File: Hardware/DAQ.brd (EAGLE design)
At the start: 44.4 x 39.7 mm, 35 parts, among them U1 DAC8564IAPW, U2 AD7606BSTZ

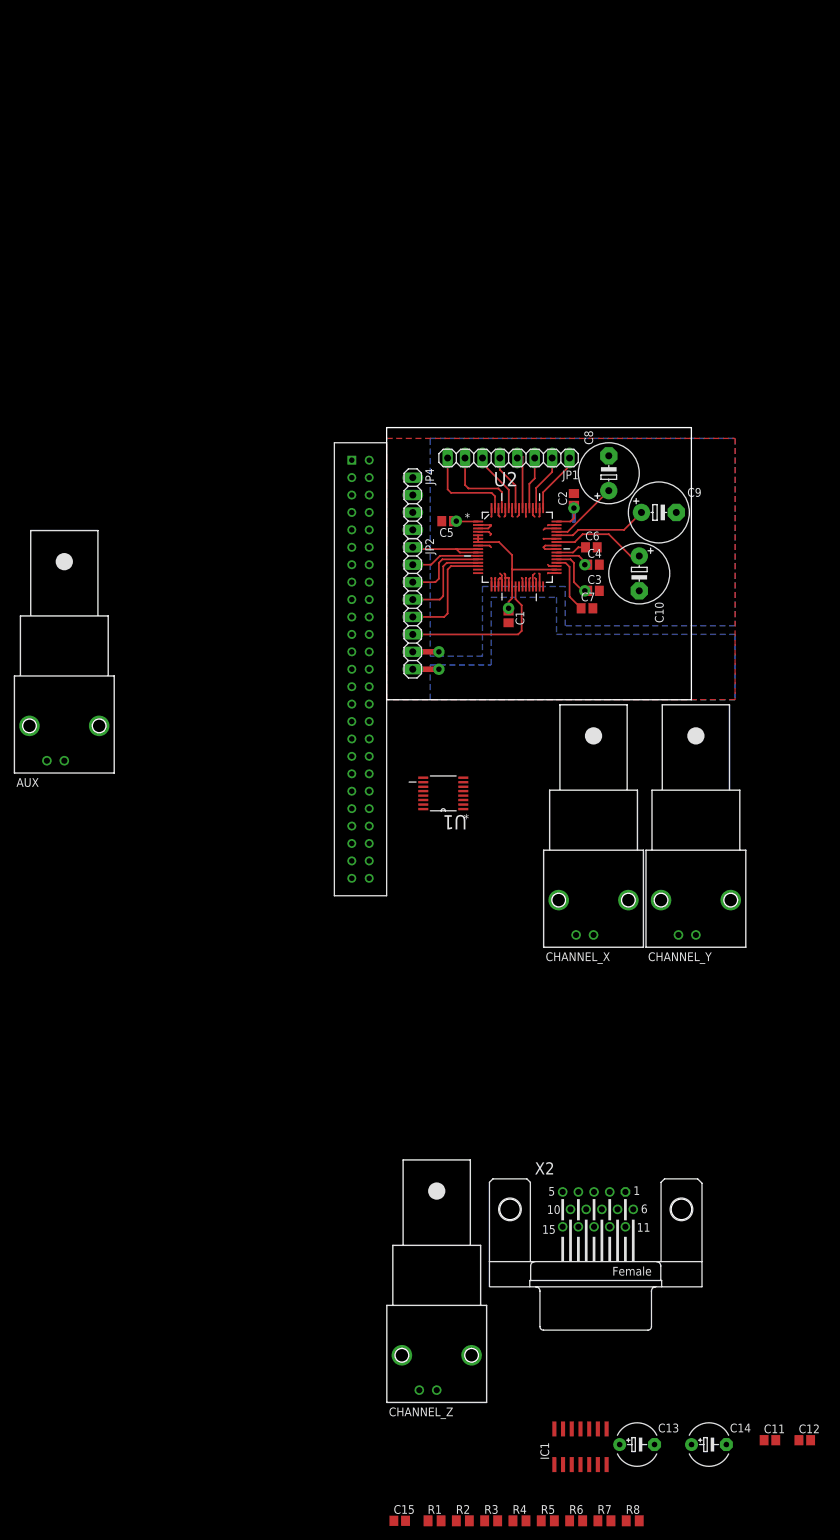
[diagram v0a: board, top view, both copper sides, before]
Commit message: added usart interface
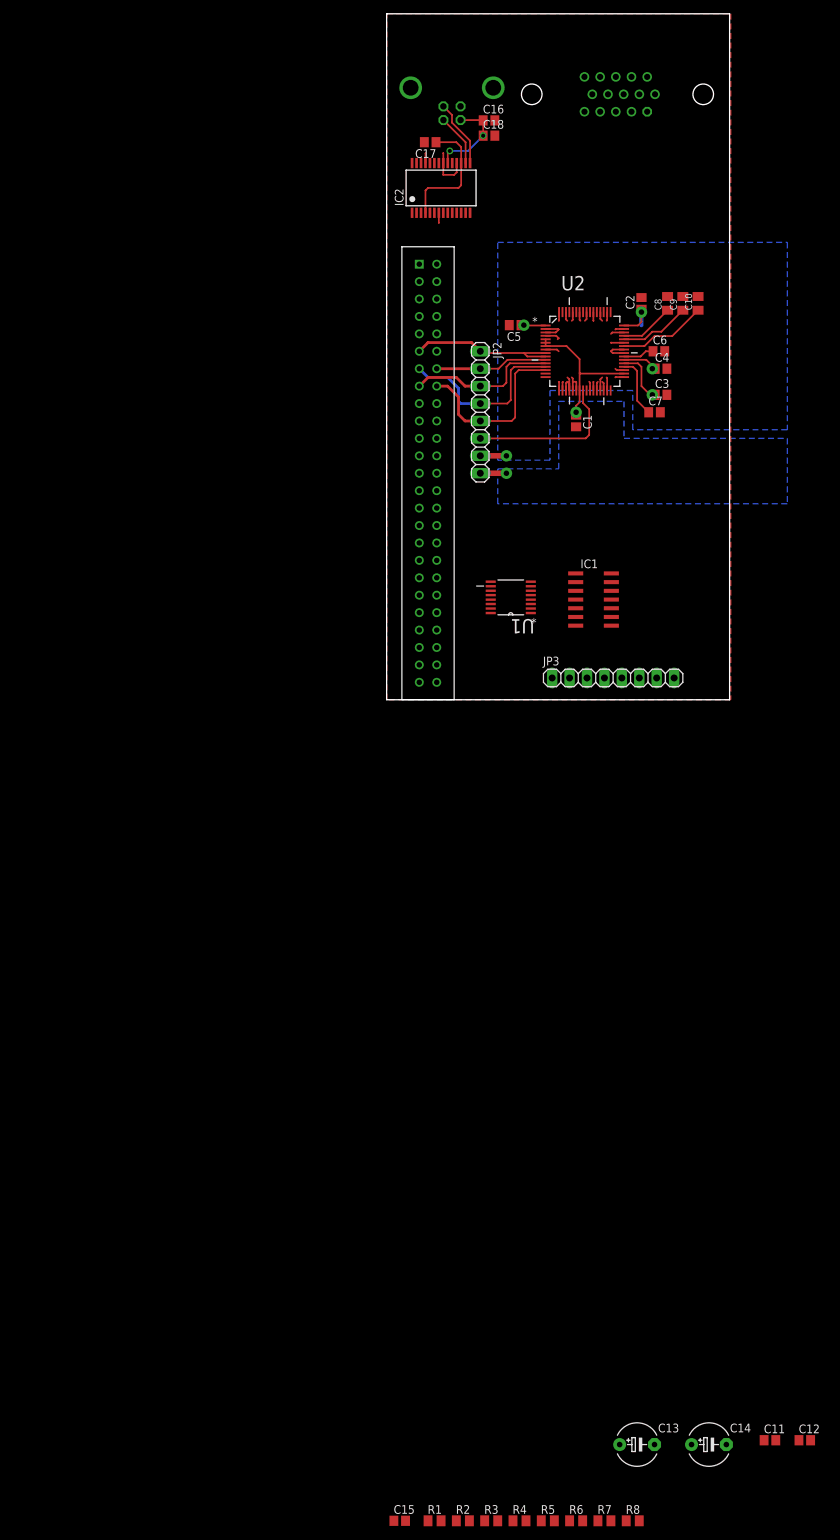
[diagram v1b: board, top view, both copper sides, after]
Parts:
- removed AUX, CHANNEL_X, CHANNEL_Y, CHANNEL_Z: (no value), con-coax:AMP_227161
- removed JP1: (no value), pinhead:1X08
- removed JP4: (no value), pinhead:1X04
- added C16, C17, C18: (no value), resistor:C0805
- added IC2: FT232RL, ftdichip:SSOP28
- added JP3: (no value), pinhead:1X08
- added X1: PN61729-S, con-berg:PN61729-S
- C10, C8, C9: device resistor:E5-8,5 -> resistor:C0805K
- moved X2 162.6 mm to (33.7, 88.3), flipped to the bottom, turned to 180 degrees
- moved IC1 123.5 mm to (30.2, 14.6), turned to 270 degrees
- moved C10 40.3 mm to (45.4, 57.8), turned to 90 degrees
- moved C9 30.7 mm to (43.2, 57.8), turned to 90 degrees
- moved C1 30.2 mm to (27.6, 40.6)
- moved C3 30.2 mm to (40.0, 44.5)
- moved U$1 30.2 mm to (6.03, 33.0)
- moved C4 30.2 mm to (40.0, 48.3)
- moved C5 30.2 mm to (18.7, 54.6)
- moved U1 30.2 mm to (18.1, 14.9)
- moved C2 30.2 mm to (37.1, 57.8)
- moved C6 30.2 mm to (39.7, 50.8)
- moved C7 30.2 mm to (39.1, 41.9)
- moved JP2 30.2 mm to (13.7, 41.9)
- moved U2 30.2 mm to (28.9, 50.8)
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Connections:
- removed net AGND: C1.2, C10.-, C2.2, C3.2, C4.2, C5.2, C6.2, C7.2, C8.-, C9.-, JP4.1, JP4.2, JP4.3, JP4.4, U2.16, U2.17, U2.18, U2.19, U2.2, U2.20, U2.21, U2.22, U2.26, U2.27, U2.28, U2.29, U2.3, U2.30, U2.31, U2.33, U2.35, U2.4, U2.40, U2.41, U2.43, U2.46, U2.47, U2.50, U2.52, U2.54, U2.56, U2.58, U2.60, U2.62, U2.64, U2.8
- removed net N$12: JP1.2, U2.51
- removed net N$13: JP1.5, U2.57
- removed net N$14: JP1.6, U2.59
- removed net N$4: JP1.3, U2.53
- removed net SP1_SCLK: JP2.3, U2.12
- net GND: now also C1.2, C10.2, C16.2, C17.2, C18.2, C2.2, C3.2, C4.2, C5.2, C6.2, C7.2, C8.2, C9.2, IC2.18, IC2.21, IC2.25, IC2.26, IC2.7, JP3.2, JP3.4, JP3.6, JP3.8, U2.16, U2.17, U2.18, U2.19, U2.2, U2.20, U2.21, U2.22, U2.26, U2.27, U2.28, U2.29, U2.3, U2.30, U2.31, U2.33, U2.35, U2.4, U2.40, U2.41, U2.43, U2.46, U2.47, U2.50, U2.52, U2.54, U2.56, U2.58, U2.60, U2.62, U2.64, U2.8, X1.4, X1.S1, X1.S2; no longer AUX.2, CHANNEL_X.2, CHANNEL_Y.2, CHANNEL_Z.2
- net N$1: now also C16.1, C18.1, IC2.20, X1.1; no longer JP1.8, U2.63
- net N$11: now also C17.1, IC2.17, IC2.4; no longer JP1.1, U2.49
- net N$15: now also C10.1; no longer C10.+
- net N$19: now also JP3.1; no longer CHANNEL_X.1
- net N$2: now also IC2.16, X1.2; no longer JP1.4, U2.55
- net N$21: now also JP3.3; no longer CHANNEL_Y.1
- net N$23: now also JP3.5; no longer CHANNEL_Z.1
- net N$25: now also JP3.7; no longer AUX.1
- net N$3: now also IC2.15, X1.3; no longer JP1.7, U2.61
- net N$8: now also C8.1; no longer C8.+
- net N$9: now also C9.1; no longer C9.+
- net Q1-Q2_BUF: now also U2.49
- net Q1-Q4_BUF: now also U2.53
- net Q1_BUF: now also U2.55
- net Q2-Q3_BUF: now also U2.63
- net Q2_BUF: now also U2.57
- net Q3_BUF: now also U2.59
- net Q4-Q3_BUF: now also U2.51
- net Q4_BUF: now also U2.61
- net SPI1_SCLK: now also JP2.3, U2.12
- net USART3_RX: now also IC2.1
- net USART3_TX: now also IC2.5
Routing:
- net GND: track 0.00 -> 60.7 mm
- net AGND: track 51.1 -> 0.00 mm
- net SPI1_SCLK: track 0.00 -> 22.8 mm
- net SP1_SCLK: track 12.3 -> 0.00 mm
- net CS: track 14.3 -> 26.4 mm
- net CONVST: track 12.9 -> 22.9 mm
- net BUSY: track 16.3 -> 26.3 mm
- net N$11: track 8.90 -> 18.3 mm
- net N$14: track 8.89 -> 0.00 mm
- net N$12: track 8.27 -> 0.00 mm
- net N$13: track 8.25 -> 0.00 mm
- net N$4: track 7.63 -> 0.00 mm
- net RESET: track 10.1 -> 16.4 mm
- net N$9: track 13.8 -> 10.3 mm
- net N$8: track 10.1 -> 7.89 mm
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- added copper zone on layer 1, net GND
- removed copper zone on layer 1, net AGND
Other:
- board size 44.4 x 39.7 mm -> 50 x 100 mm

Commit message: finished board layout
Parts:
- removed JP2: (no value), pinhead:1X08
- added C19, C20, C21, C22, C23, C24, C25, C26: (no value), resistor:C0805K
- added D1: 1N4004, diode:DO41-10
- added IC3, IC4, IC5: MCP1703DB, linear:SOT223
- added JP1: (no value), pinhead:1X02
- added JP4: (no value), pinhead:1X03
- C13, C14: device resistor:E5-6 -> resistor:C0805
- moved C15 149.7 mm to (17.1, 29.2), turned to 180 degrees
- moved R7 144.0 mm to (38.1, 24.1), turned to 270 degrees
- moved R8 143.9 mm to (40.3, 24.1), turned to 90 degrees
- moved R1 143.7 mm to (27.3, 22.5), turned to 90 degrees
- moved R2 142.9 mm to (25.1, 22.5), turned to 270 degrees
- moved C12 142.7 mm to (31.8, 31.8)
- moved C14 139.0 mm to (31.8, 29.5)
- moved C11 137.4 mm to (31.8, 27.3)
- moved C13 136.9 mm to (17.1, 27.0), turned to 180 degrees
- moved R3 135.2 mm to (27.3, 14.9), turned to 90 degrees
- moved R4 134.7 mm to (25.1, 14.9), turned to 270 degrees
- moved R5 134.1 mm to (38.1, 13.7), turned to 270 degrees
- moved R6 134.0 mm to (40.3, 13.7), turned to 90 degrees
- moved U1 16.0 mm to (23.8, 29.8)
- moved C7 14.9 mm to (39.1, 56.8)
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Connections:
- removed net V+: IC1.4
- removed net V-: IC1.11
- new net N$12: C21.1, IC5.3, JP1.1
- new net N$29: C22.1, C23.1, C24.1, D1.C, IC3.1, IC4.1, IC5.1
- net +15V: now also C25.1, D1.A, IC1.4, JP4.1
- net +3V3: now also C13.1, C14.1, C20.1, IC3.3; no longer C13.+, C14.+, JP2.8
- net +5V: now also C19.1, IC4.3; no longer JP2.7
- net -15V: now also C26.1, IC1.11, JP4.3
- net BUSY: no longer JP2.5
- net CONVST: no longer JP2.1
- net CS: no longer JP2.4
- net GND: now also C13.2, C14.2, C19.2, C20.2, C21.2, C22.2, C23.2, C24.2, C25.2, C26.2, IC3.2, IC4.2, IC5.2, JP1.2, JP4.2; no longer C13.-, C14.-
- net RESET: no longer JP2.2
- net SPI1_MISO: no longer JP2.6
- net SPI1_SCLK: no longer JP2.3
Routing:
- net +15V: track 0.00 -> 145.9 mm, vias 0 -> 2
- net -15V: track 0.00 -> 118.2 mm, vias 0 -> 1
- net N$29: track 0.00 -> 72.5 mm, vias 0 -> 2
- net USART3_TX: track 0.00 -> 63.3 mm
- net USART3_RX: track 0.00 -> 60.7 mm
- net N$25: track 0.00 -> 47.7 mm
- net N$19: track 0.00 -> 34.4 mm
- net SPI2_MOSI: track 0.00 -> 31.0 mm
- net Q4_BUF: track 0.00 -> 29.5 mm
- net N$16: track 0.00 -> 29.4 mm, vias 0 -> 2
- net SPI2_SCLK: track 0.00 -> 29.1 mm
- net Q3_BUF: track 0.00 -> 28.2 mm
- net ~SYNC: track 0.00 -> 27.2 mm
- net N$17: track 0.00 -> 27.2 mm, vias 0 -> 2
- net Q2-Q3_BUF: track 0.00 -> 26.3 mm, vias 0 -> 1
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- added copper zone on layer 16, net GND

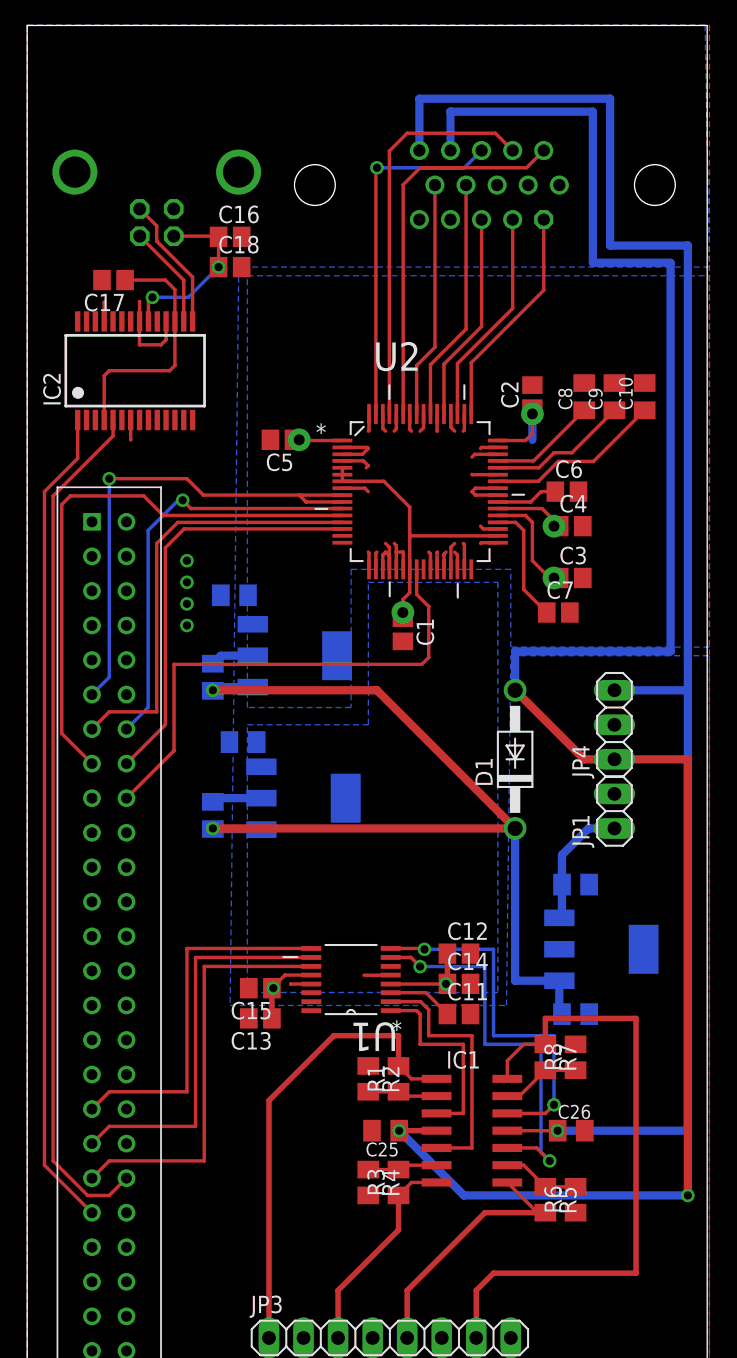
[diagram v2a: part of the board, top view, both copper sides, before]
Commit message: added HP GPIB Arduino controller
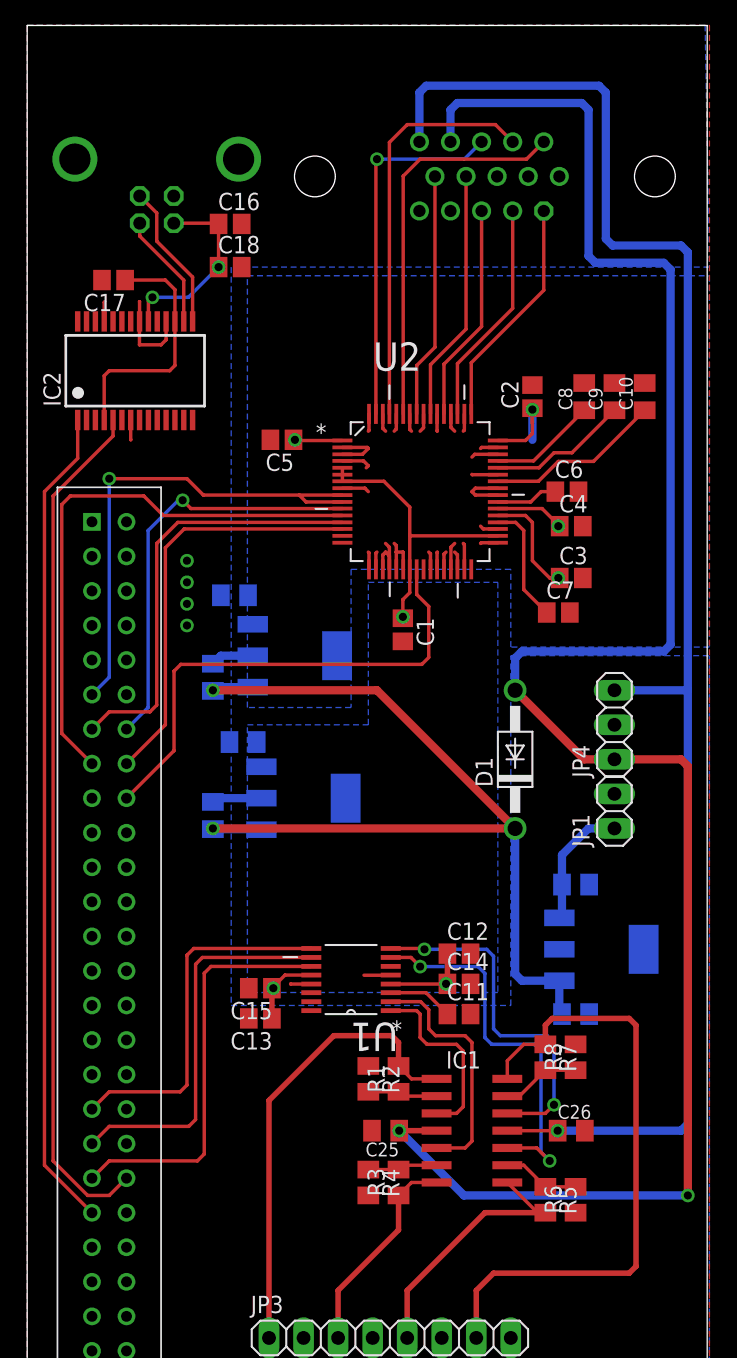
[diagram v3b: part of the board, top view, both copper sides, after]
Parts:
- moved C16 0.95 mm to (14.9, 85.4)
- moved X1 0.95 mm to (9.53, 90.2)
- moved X2 0.64 mm to (33.7, 88.9)
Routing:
- net +15V: track 145.9 -> 144.5 mm
- net N$3: track 9.88 -> 10.8 mm
- net N$2: track 7.61 -> 8.56 mm
- net N$1: track 13.2 -> 14.2 mm
- net N$25: track 47.7 -> 46.8 mm
- net N$17: track 27.2 -> 26.3 mm
- net N$5: track 14.7 -> 13.8 mm
- net N$6: track 19.0 -> 18.1 mm
- net N$16: track 29.4 -> 28.5 mm
- net Q4-Q3_BUF: track 16.0 -> 16.6 mm
- net Q2_BUF: track 17.4 -> 18.0 mm
- net Q1_BUF: track 17.9 -> 18.5 mm
- net Q1-Q4_BUF: track 15.4 -> 16.1 mm
- net Q1-Q2_BUF: track 16.5 -> 17.1 mm
- net Q2-Q3_BUF: track 26.3 -> 27.0 mm
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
